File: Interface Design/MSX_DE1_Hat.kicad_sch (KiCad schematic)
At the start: 24 parts, among them J1 J1, J2 J2, J3 J3, J4 J4, J5 J5, J6 J6, U1 74LVC245A, U2 74LVC245A, U3 74LVC245A, U4 74LVC245A, U5 74LVC245A

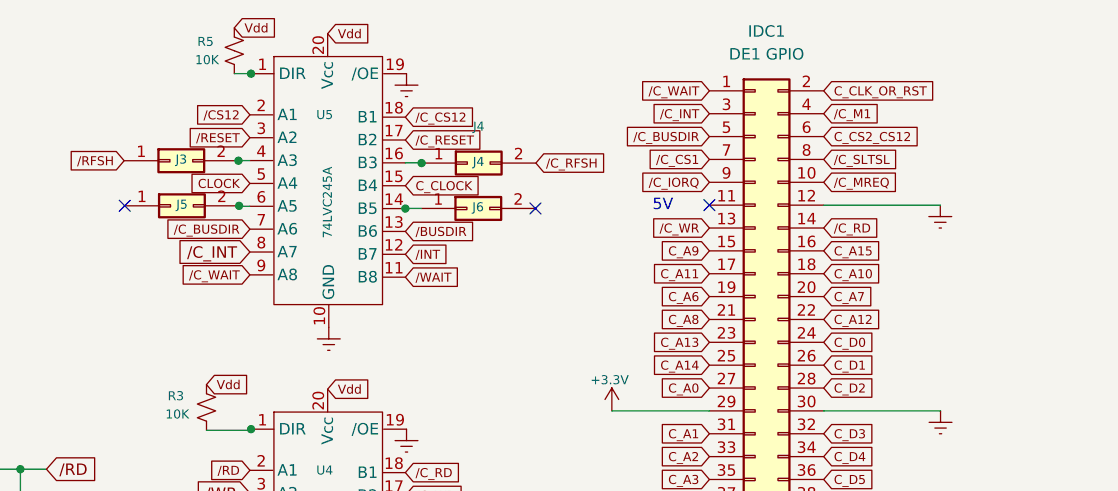
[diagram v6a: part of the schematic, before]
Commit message: Compatibel with DE0 & DE1
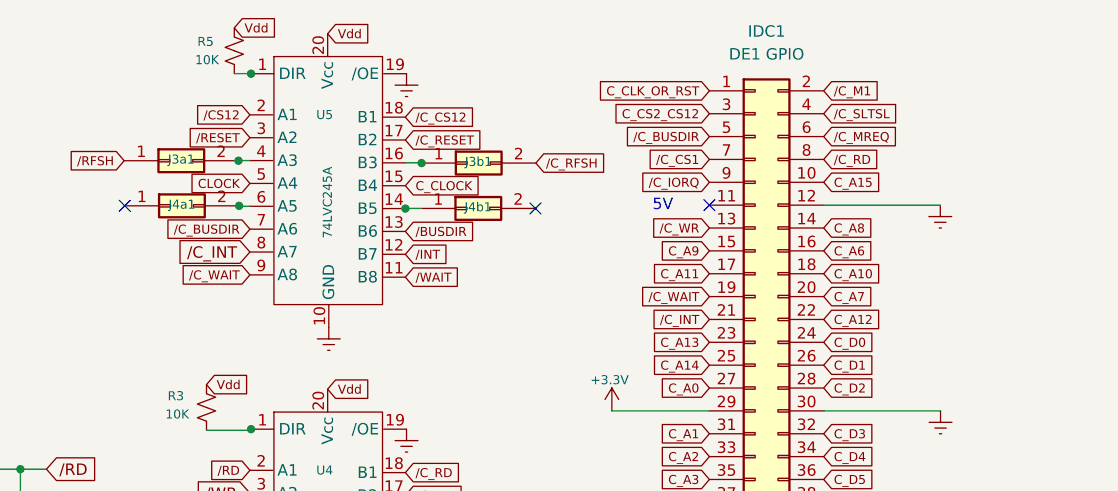
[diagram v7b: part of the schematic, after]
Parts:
- J3a1: renamed from J3; value J3 -> J3a
- J3b1: renamed from J4; value J4 -> J3b
- J4a1: renamed from J5; value J5 -> J4a
- J4b1: renamed from J6; value J6 -> J4b
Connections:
- net C_A15: now also IDC1.10 (Pin_10); no longer IDC1.16 (Pin_16)
- net C_A6: now also IDC1.16 (Pin_16); no longer IDC1.19 (Pin_19)
- net C_A8: now also IDC1.14 (Pin_14); no longer IDC1.21 (Pin_21)
- net C_CLK_OR_RST: now also IDC1.1 (Pin_1); no longer IDC1.2 (Pin_2)
- net C_CS2_CS12: now also IDC1.3 (Pin_3); no longer IDC1.6 (Pin_6)
- net /C_INT: now also IDC1.21 (Pin_21); no longer IDC1.3 (Pin_3)
- net /C_M1: now also IDC1.2 (Pin_2); no longer IDC1.4 (Pin_4)
- net /C_MREQ: now also IDC1.6 (Pin_6); no longer IDC1.10 (Pin_10)
- net /C_RD: now also IDC1.8 (Pin_8); no longer IDC1.14 (Pin_14)
- net /C_SLTSL: now also IDC1.4 (Pin_4); no longer IDC1.8 (Pin_8)
- net /C_WAIT: now also IDC1.19 (Pin_19); no longer IDC1.1 (Pin_1)
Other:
- title: MSX DE1 Hat -> MSX FPGA Hat
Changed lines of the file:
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@@
   (paper "A4" portrait)
   (title_block
-    (title "MSX DE1 Hat")
-    (date "2023-01-09")
+    (title "MSX FPGA Hat")
+    (date "2023-01-17")
     (rev "1.1")
     (company "RCC")
@@
     (comment 2 "Cartridge for MSX Computers that expose the MSX BUS")
     (comment 3 "IDC connector pinout mapped for Altera DE1 FPGA Development Board")
+    (comment 4 "Designed for Terasic DE0 & DE1")
   )
   (junction (at 127.508 157.48) (diameter 0) (color 0 0 0 0)
@@
     )
   )
-  (global_label "{slash}C_SLTSL" (shape input) (at 136.906 56.388 0) (fields_autoplaced)
-    (effects (font (size 1 1)) (justify left))
-    (property "Intersheet References" "${INTERSHEET_REFS}" (id 0) (at 143.2027 56.3443 0)
+  (global_label "{slash}C_SLTSL" (shape input) (at 136.906 51.308 0) (fields_autoplaced)
+    (effects (font (size 1 1)) (justify left))
+    (property "Intersheet References" "${INTERSHEET_REFS}" (id 0) (at 143.2027 51.2643 0)
       (effects (font (size 1 1)) (justify left) hide)
     )
@@
     )
   )
-  (global_label "C_CS2_CS12" (shape input) (at 136.906 53.848 0) (fields_autoplaced)
-    (effects (font (size 1 1)) (justify left))
-    (property "Intersheet References" "${INTERSHEET_REFS}" (id 0) (at 148.0917 53.7855 0)
-      (effects (font (size 1 1)) (justify left) hide)
+  (global_label "C_CS2_CS12" (shape input) (at 124.206 51.308 180) (fields_autoplaced)
+    (effects (font (size 1 1)) (justify right))
+    (property "Intersheet References" "${INTERSHEET_REFS}" (id 0) (at 113.0203 51.3705 0)
+      (effects (font (size 1 1)) (justify right) hide)
     )
   )
@@
     )
   )
-  (global_label "{slash}C_M1" (shape input) (at 136.906 51.308 0) (fields_autoplaced)
-    (effects (font (size 1 1)) (justify left))
-    (property "Intersheet References" "${INTERSHEET_REFS}" (id 0) (at 141.6693 51.2643 0)
+  (global_label "{slash}C_M1" (shape input) (at 136.906 48.768 0) (fields_autoplaced)
+    (effects (font (size 1 1)) (justify left))
+    (property "Intersheet References" "${INTERSHEET_REFS}" (id 0) (at 141.6693 48.7243 0)
       (effects (font (size 1 1)) (justify left) hide)
     )
@@
     )
   )
-  (global_label "C_A8" (shape input) (at 124.206 74.168 180) (fields_autoplaced)
-    (effects (font (size 1 1)) (justify right))
-    (property "Intersheet References" "${INTERSHEET_REFS}" (id 0) (at 120.376 74.2117 0)
-      (effects (font (size 1 1)) (justify right) hide)
+  (global_label "C_A8" (shape input) (at 136.906 64.008 0) (fields_autoplaced)
+    (effects (font (size 1 1)) (justify left))
+    (property "Intersheet References" "${INTERSHEET_REFS}" (id 0) (at 140.736 63.9643 0)
+      (effects (font (size 1 1)) (justify left) hide)
     )
   )
@@
     )
   )
-  (global_label "C_A15" (shape input) (at 136.906 66.548 0) (fields_autoplaced)
-    (effects (font (size 1 1)) (justify left))
-    (property "Intersheet References" "${INTERSHEET_REFS}" (id 0) (at 141.4027 66.5043 0)
+  (global_label "C_A15" (shape input) (at 136.906 58.928 0) (fields_autoplaced)
+    (effects (font (size 1 1)) (justify left))
+    (property "Intersheet References" "${INTERSHEET_REFS}" (id 0) (at 141.4027 58.8843 0)
       (effects (font (size 1 1)) (justify left) hide)
     )
@@
     )
   )
-  (global_label "C_A6" (shape input) (at 124.206 71.628 180) (fields_autoplaced)
-    (effects (font (size 1 1)) (justify right))
-    (property "Intersheet References" "${INTERSHEET_REFS}" (id 0) (at 120.376 71.6717 0)
-      (effects (font (size 1 1)) (justify right) hide)
+  (global_label "C_A6" (shape input) (at 136.906 66.548 0) (fields_autoplaced)
+    (effects (font (size 1 1)) (justify left))
+    (property "Intersheet References" "${INTERSHEET_REFS}" (id 0) (at 140.736 66.5043 0)
+      (effects (font (size 1 1)) (justify left) hide)
     )
   )
@@
     )
   )
-  (global_label "{slash}C_INT" (shape input) (at 124.206 51.308 180) (fields_autoplaced)
-    (effects (font (size 1 1)) (justify right))
-    (property "Intersheet References" "${INTERSHEET_REFS}" (id 0) (at 117.2108 51.2455 0)
+  (global_label "{slash}C_INT" (shape input) (at 124.206 74.168 180) (fields_autoplaced)
+    (effects (font (size 1 1)) (justify right))
+    (property "Intersheet References" "${INTERSHEET_REFS}" (id 0) (at 117.2108 74.1055 0)
       (effects (font (size 1 1)) (justify right) hide)
     )
@@
     )
   )
-  (global_label "{slash}C_MREQ" (shape input) (at 136.906 58.928 0) (fields_autoplaced)
-    (effects (font (size 1 1)) (justify left))
-    (property "Intersheet References" "${INTERSHEET_REFS}" (id 0) (at 143.0693 58.8843 0)
+  (global_label "{slash}C_MREQ" (shape input) (at 136.906 53.848 0) (fields_autoplaced)
+    (effects (font (size 1 1)) (justify left))
+    (property "Intersheet References" "${INTERSHEET_REFS}" (id 0) (at 143.0693 53.8043 0)
       (effects (font (size 1 1)) (justify left) hide)
     )
@@
     )
   )
-  (global_label "{slash}C_RD" (shape input) (at 136.906 64.008 0) (fields_autoplaced)
-    (effects (font (size 1 1)) (justify left))
-    (property "Intersheet References" "${INTERSHEET_REFS}" (id 0) (at 141.6027 63.9643 0)
+  (global_label "{slash}C_RD" (shape input) (at 136.906 56.388 0) (fields_autoplaced)
+    (effects (font (size 1 1)) (justify left))
+    (property "Intersheet References" "${INTERSHEET_REFS}" (id 0) (at 141.6027 56.3443 0)
       (effects (font (size 1 1)) (justify left) hide)
     )
@@
     )
   )
-  (global_label "{slash}C_WAIT" (shape input) (at 124.206 48.768 180) (fields_autoplaced)
-    (effects (font (size 1 1)) (justify right))
-    (property "Intersheet References" "${INTERSHEET_REFS}" (id 0) (at 118.6427 48.8117 0)
+  (global_label "{slash}C_WAIT" (shape input) (at 124.206 71.628 180) (fields_autoplaced)
+    (effects (font (size 1 1)) (justify right))
+    (property "Intersheet References" "${INTERSHEET_REFS}" (id 0) (at 118.6427 71.6717 0)
       (effects (font (size 1 1)) (justify right) hide)
     )
@@
     )
   )
-  (global_label "C_CLK_OR_RST" (shape input) (at 136.906 48.768 0) (fields_autoplaced)
-    (effects (font (size 1 1)) (justify left))
-    (property "Intersheet References" "${INTERSHEET_REFS}" (id 0) (at 149.6631 48.7055 0)
-      (effects (font (size 1 1)) (justify left) hide)
+  (global_label "C_CLK_OR_RST" (shape input) (at 124.206 48.768 180) (fields_autoplaced)
+    (effects (font (size 1 1)) (justify right))
+    (property "Intersheet References" "${INTERSHEET_REFS}" (id 0) (at 111.4489 48.8305 0)
+      (effects (font (size 1 1)) (justify right) hide)
     )
   )
@@
   (symbol (lib_id "Connector_Generic:Conn_02x01") (at 97.3044 56.7906 0) (unit 1)
     (in_bom yes) (on_board yes)
-    (property "Reference" "J4" (id 0) (at 98.552 56.642 0)
+    (property "Reference" "J3b1" (id 0) (at 98.552 56.642 0)
       (effects (font (size 1 1)))
     )
-    (property "Value" "J4" (id 1) (at 98.5744 52.7266 0)
-      (effects (font (size 1 1)))
+    (property "Value" "J3b" (id 1) (at 98.5744 52.7266 0)
+      (effects (font (size 1 1)) hide)
     )
     (property "Footprint" "Connector_PinHeader_2.54mm:PinHeader_1x02_P2.54mm_Vertical" (id 2) (at 97.3044 56.7906 0)
@@
   (symbol (lib_id "Connector_Generic:Conn_02x01") (at 64.257 56.5317 0) (unit 1)
     (in_bom yes) (on_board yes)
-    (property "Reference" "J3" (id 0) (at 65.532 56.388 0)
+    (property "Reference" "J3a1" (id 0) (at 65.532 56.388 0)
       (effects (font (size 1 1)))
     )
-    (property "Value" "J3" (id 1) (at 65.527 52.4677 0)
+    (property "Value" "J3a" (id 1) (at 65.527 52.4677 0)
       (effects (font (size 1 1)) hide)
     )
@@
   (symbol (lib_id "Connector_Generic:Conn_02x01") (at 97.258 61.8336 0) (unit 1)
     (in_bom yes) (on_board yes)
-    (property "Reference" "J6" (id 0) (at 98.5056 61.685 0)
+    (property "Reference" "J4b1" (id 0) (at 98.5056 61.685 0)
       (effects (font (size 1 1)))
     )
-    (property "Value" "J6" (id 1) (at 98.528 57.7696 0)
+    (property "Value" "J4b" (id 1) (at 98.528 57.7696 0)
       (effects (font (size 1 1)) hide)
     )
@@
   (symbol (lib_id "Connector_Generic:Conn_02x01") (at 64.3266 61.5421 0) (unit 1)
     (in_bom yes) (on_board yes)
-    (property "Reference" "J5" (id 0) (at 65.6016 61.3984 0)
+    (property "Reference" "J4a1" (id 0) (at 65.6016 61.3984 0)
       (effects (font (size 1 1)))
     )
-    (property "Value" "J5" (id 1) (at 65.5966 57.4781 0)
+    (property "Value" "J4a" (id 1) (at 65.5966 57.4781 0)
       (effects (font (size 1 1)) hide)
     )
@@
     )
     (path "/4042273a-f49c-4fe5-b27e-5b6a5cdf93be"
-      (reference "J3") (unit 1) (value "J3") (footprint "Connector_PinHeader_2.54mm:PinHeader_1x02_P2.54mm_Vertical")
+      (reference "J3a1") (unit 1) (value "J3a") (footprint "Connector_PinHeader_2.54mm:PinHeader_1x02_P2.54mm_Vertical")
     )
     (path "/319b83ec-d671-46f4-8155-38e9eb95b6e6"
-      (reference "J4") (unit 1) (value "J4") (footprint "Connector_PinHeader_2.54mm:PinHeader_1x02_P2.54mm_Vertical")
+      (reference "J3b1") (unit 1) (value "J3b") (footprint "Connector_PinHeader_2.54mm:PinHeader_1x02_P2.54mm_Vertical")
     )
     (path "/f68c91da-d3d4-4cee-8cb1-d5a368c40e28"
-      (reference "J5") (unit 1) (value "J5") (footprint "Connector_PinHeader_2.54mm:PinHeader_1x02_P2.54mm_Vertical")
+      (reference "J4a1") (unit 1) (value "J4a") (footprint "Connector_PinHeader_2.54mm:PinHeader_1x02_P2.54mm_Vertical")
     )
     (path "/e3f72cd2-342f-474f-a016-7c306e08e4bc"
-      (reference "J6") (unit 1) (value "J6") (footprint "Connector_PinHeader_2.54mm:PinHeader_1x02_P2.54mm_Vertical")
+      (reference "J4b1") (unit 1) (value "J4b") (footprint "Connector_PinHeader_2.54mm:PinHeader_1x02_P2.54mm_Vertical")
     )
     (path "/75b8a547-7dbb-4ae6-a265-87342b091832"
